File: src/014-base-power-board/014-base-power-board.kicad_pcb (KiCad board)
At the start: 2 copper layers, 20 x 40 mm, 16 parts, among them J1 GND, J10 V4, J2 GND, J3 V1, J4 V1, J5 V2, J6 V2, J7 V3, J8 V3, J9 V4

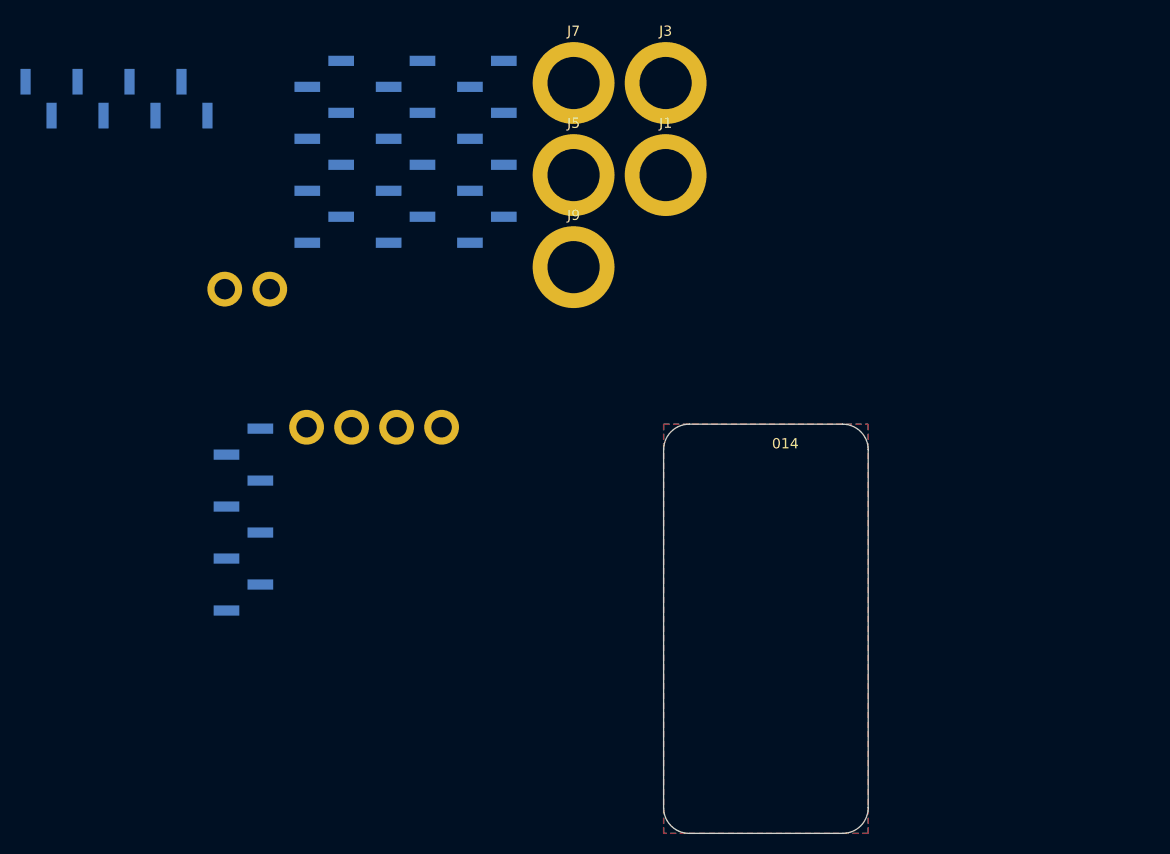
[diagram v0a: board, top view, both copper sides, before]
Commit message: Adding 014-base-power-board
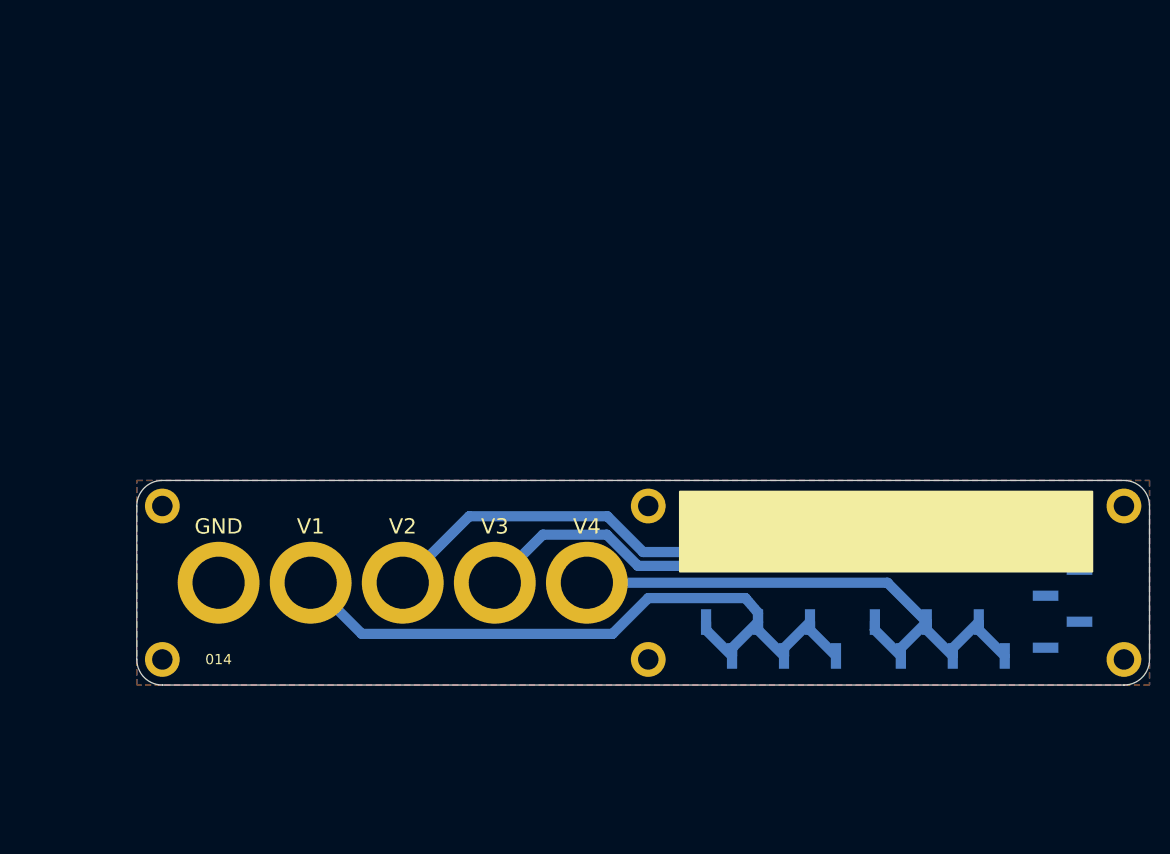
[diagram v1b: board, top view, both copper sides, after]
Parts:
- added G***: LOGO, LOGO, F.Cu at (156.0, 95.0)
- J10, J2, J4, J6, J8: footprint Connector_PinHeader_2.54mm:PinHeader_1x08_P2.54mm_Vertical_SMD_Pin1Left -> Connector_PinHeader_2.54mm:PinHeader_1x06_P2.54mm_Vertical_SMD_Pin1Left
- moved J8 90.7 mm to (177.0, 85.0), turned to 90 degrees
- moved H4 83.1 mm to (195.0, 98.0)
- moved J2 80.3 mm to (189.0, 90.5)
- moved J10 76.7 mm to (177.0, 96.0), turned to 90 degrees
- moved H3 67.1 mm to (195.0, 83.0)
- moved J3 59.9 mm to (115.5, 90.5)
- moved J1 59.1 mm to (106.5, 90.5)
- moved J4 55.1 mm to (160.5, 96.0), turned to 90 degrees
- moved H5 55.0 mm to (148.5, 98.0)
- moved J6 51.2 mm to (160.5, 85.0), turned to 90 degrees
- moved J7 49.5 mm to (133.5, 90.5)
- moved J5 43.2 mm to (124.5, 90.5)
- moved H6 37.7 mm to (101.0, 98.0)
- moved J9 30.9 mm to (142.5, 90.5)
- moved H2 25.8 mm to (148.5, 83.0)
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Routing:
- net Net-(J7-Pad1): track 0.00 -> 70.7 mm
- net Net-(J3-Pad1): track 0.00 -> 70.6 mm
- net Net-(J5-Pad1): track 0.00 -> 58.5 mm
- net Net-(J10-Pad1): track 0.00 -> 56.6 mm
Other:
- board size 20 x 40 mm -> 99 x 20 mm
- board text added: "GND"
- board text added: "Modular RF Bench Jakub Niemczuk github.com/Halogenek/modular-rf-bench"
- board text added: "V1"
- board text added: "V2"
- board text added: "V3"
- board text added: "V4"
